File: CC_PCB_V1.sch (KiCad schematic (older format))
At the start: 9 parts, among them J1 Screw_Terminal_01x07, J2 Antenna_Conn_02x04_Odd_Even, J3 USB1130-15-A_REVA, J5 Relay_Conn_01x06, U1 Pico, U2 LM337_TO3

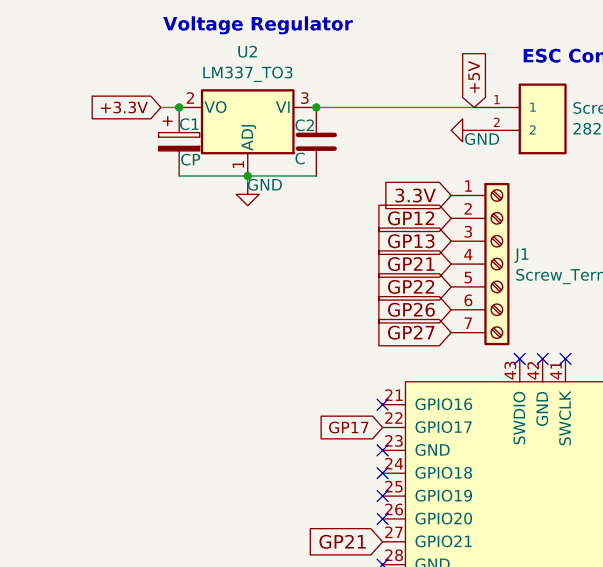
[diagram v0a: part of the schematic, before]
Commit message: Added 1x2 screw terminal for the POTS
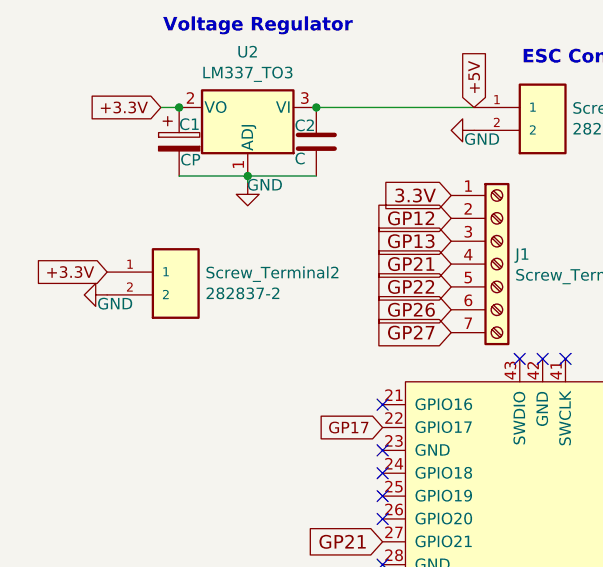
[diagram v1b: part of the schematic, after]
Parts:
- added Screw_Terminal2: 282837-2, MCU_RaspberryPi_and_Boards:TE_282837-2, symbol 282837-2:282837-2
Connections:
- net +3.3V: now also Screw_Terminal2.1
- net GND: now also Screw_Terminal2.2
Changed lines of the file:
@@
 $EndComp
 NoConn ~ 6620 2600
+$Comp
+L 282837-2:282837-2 Screw_Terminal2
+U 1 1 614A273C
+P 3215 2910
+F 0 "Screw_Terminal2" H 3345 2906 50  0000 L CNN
+F 1 "282837-2" H 3345 2815 50  0000 L CNN
+F 2 "MCU_RaspberryPi_and_Boards:TE_282837-2" H 3215 2910 50  0001 L BNN
+F 3 "" H 3215 2910 50  0001 L BNN
+F 4 "282837-2" H 3215 2910 50  0001 L BNN "Comment"
+	1    3215 2910
+	1    0    0    -1
+$EndComp
+$Comp
+L power:GND #PWR0107
+U 1 1 614A47B6
+P 2915 3010
+F 0 "#PWR0107" H 2915 2760 50  0001 C CNN
+F 1 "GND" V 2955 3045 50  0000 C CNN
+F 2 "" H 2915 3010 50  0001 C CNN
+F 3 "" H 2915 3010 50  0001 C CNN
+	1    2915 3010
+	0    1    1    0
+$EndComp
+Text GLabel 2915 2910 0    50   Input ~ 0
++3.3V
 $EndSCHEMATC

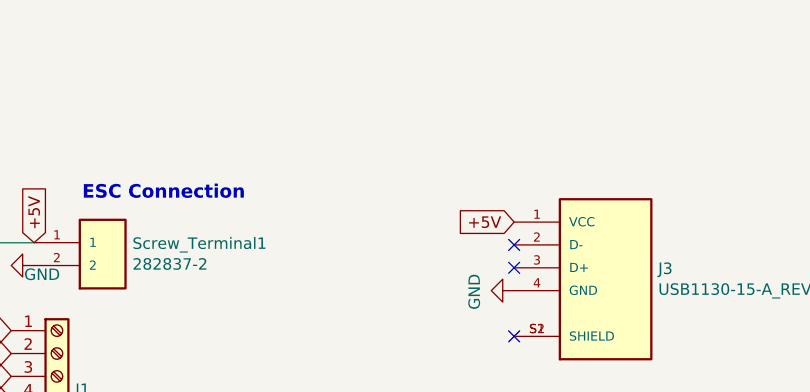
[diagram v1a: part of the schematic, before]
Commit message: Added mounting holes
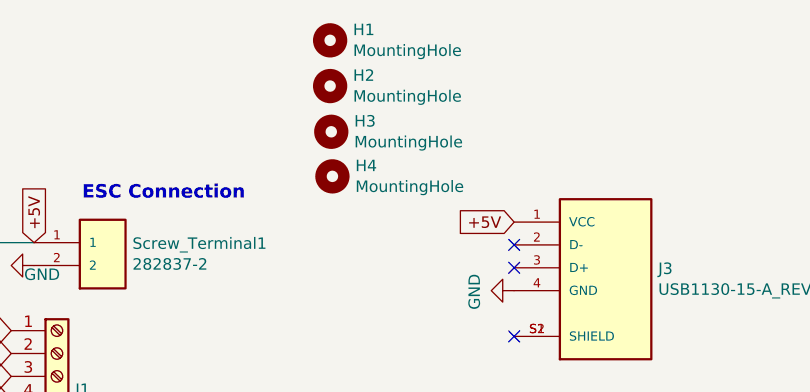
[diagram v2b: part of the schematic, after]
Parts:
- added H1, H2, H3, H4: MountingHole, MountingHole:MountingHole_3mm, symbol Mechanical:MountingHole
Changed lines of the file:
@@
 Text GLabel 2915 2910 0    50   Input ~ 0
 +3.3V
+$Comp
+L Mechanical:MountingHole H1
+U 1 1 614A4A29
+P 5815 1305
+F 0 "H1" H 5915 1351 50  0000 L CNN
+F 1 "MountingHole" H 5915 1260 50  0000 L CNN
+F 2 "MountingHole:MountingHole_3mm" H 5815 1305 50  0001 C CNN
+F 3 "~" H 5815 1305 50  0001 C CNN
+	1    5815 1305
+	1    0    0    -1
+$EndComp
+$Comp
+L Mechanical:MountingHole H2
+U 1 1 614A5922
+P 5815 1505
+F 0 "H2" H 5915 1551 50  0000 L CNN
+F 1 "MountingHole" H 5915 1460 50  0000 L CNN
+F 2 "MountingHole:MountingHole_3mm" H 5815 1505 50  0001 C CNN
+F 3 "~" H 5815 1505 50  0001 C CNN
+	1    5815 1505
+	1    0    0    -1
+$EndComp
+$Comp
+L Mechanical:MountingHole H3
+U 1 1 614A5C32
+P 5820 1705
+F 0 "H3" H 5920 1751 50  0000 L CNN
+F 1 "MountingHole" H 5920 1660 50  0000 L CNN
+F 2 "MountingHole:MountingHole_3mm" H 5820 1705 50  0001 C CNN
+F 3 "~" H 5820 1705 50  0001 C CNN
+	1    5820 1705
+	1    0    0    -1
+$EndComp
+$Comp
+L Mechanical:MountingHole H4
+U 1 1 614A5FD8
+P 5825 1900
+F 0 "H4" H 5925 1946 50  0000 L CNN
+F 1 "MountingHole" H 5925 1855 50  0000 L CNN
+F 2 "MountingHole:MountingHole_3mm" H 5825 1900 50  0001 C CNN
+F 3 "~" H 5825 1900 50  0001 C CNN
+	1    5825 1900
+	1    0    0    -1
+$EndComp
 $EndSCHEMATC
